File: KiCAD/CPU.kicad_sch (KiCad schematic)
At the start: 28 parts

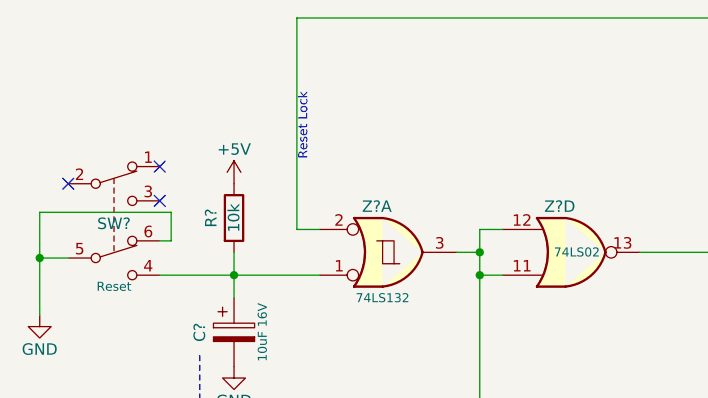
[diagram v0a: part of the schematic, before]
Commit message: Update schematics (correct page flow) and add alternative to Q4 in BOM
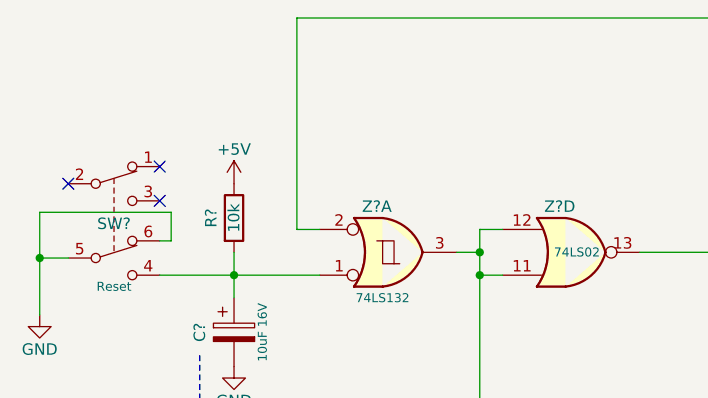
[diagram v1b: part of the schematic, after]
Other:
- note removed: "Reset Lock"
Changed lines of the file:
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@@
-    (effects (font (size 1 1)) (justify left bottom))
-  )
-  (text "Reset Lock" (at 49.53 40.005 90)
     (effects (font (size 1 1)) (justify left bottom))
   )

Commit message: Updated revision to Rev C
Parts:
- gave numbers to parts that had none: 16
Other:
- title: TRS-80 Model I G -> TRS-80 Model I Rev G
